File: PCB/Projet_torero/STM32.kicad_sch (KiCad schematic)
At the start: 34 parts, among them J1 Conn_02x07_Odd_Even, J201 Conn_02x08_Odd_Even, SW1 SW_Push, SW2 SW_Push, U1 STM32G431CBUx, Y1 Crystal_GND24_Small

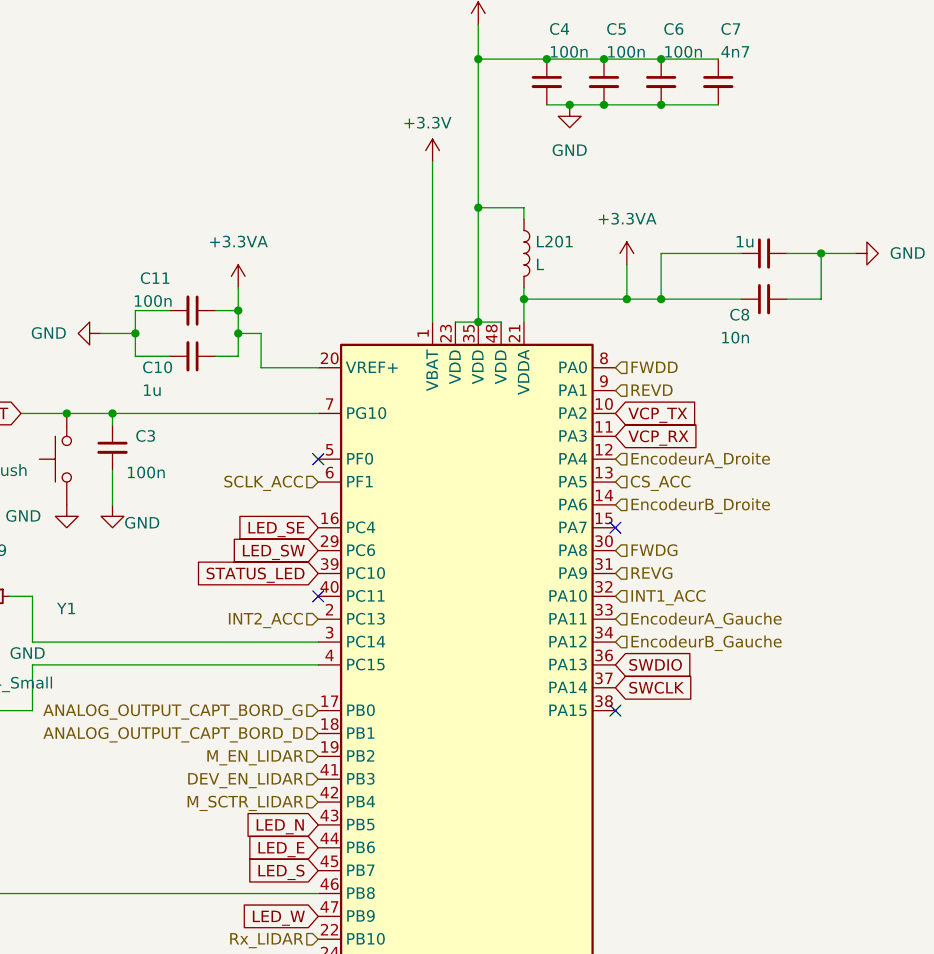
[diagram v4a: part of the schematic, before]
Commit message: changement pins STlink
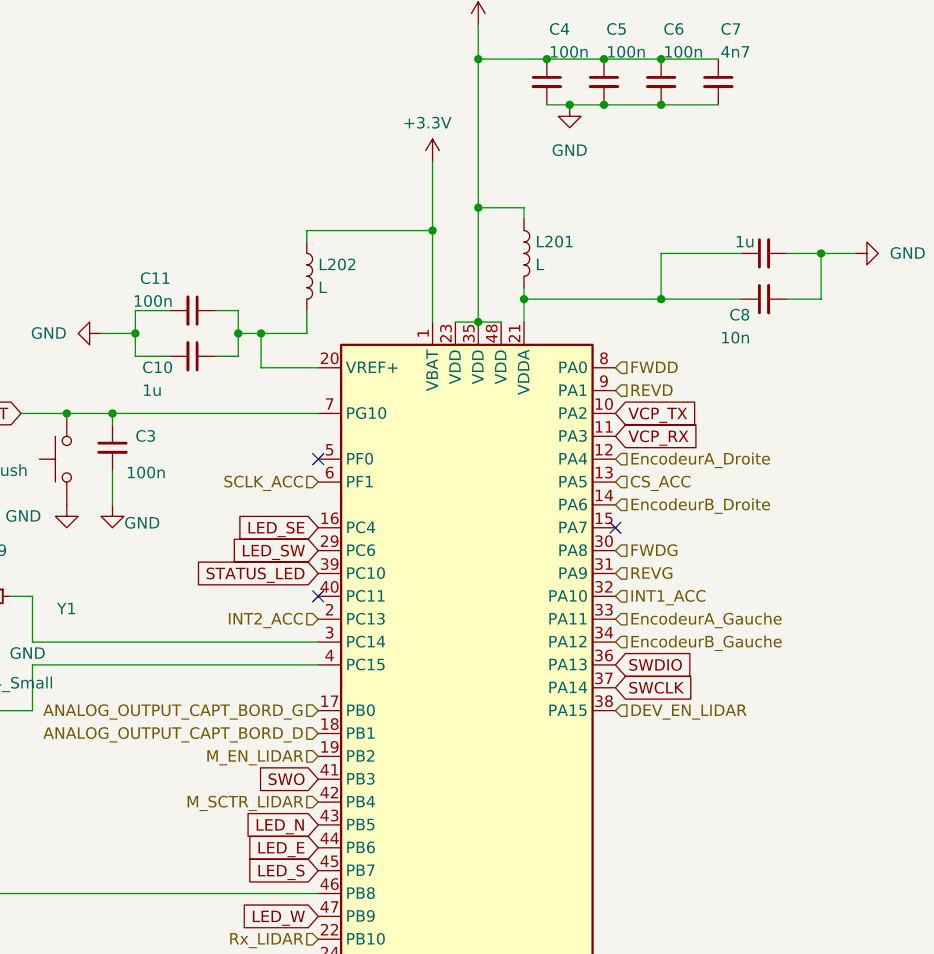
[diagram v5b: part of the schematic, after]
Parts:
- added L202: L, symbol Device:L
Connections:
- net +3.3V: now also L202.1
- net DEV_EN_LIDAR: now also U1.38 (PA15); no longer U1.41 (PB3)
- net SWO: now also U1.41 (PB3)
- net +3.3VA: no longer names the net of C8.1, C9.1, L201.2, U1.21 (VDDA)
- net +3.3VA: no longer C10.1, C11.1, U1.20 (VREF+)
- new net: C10.1, C11.1, L202.2, U1.20 (VREF+)
- no-connect marks 8 -> 7
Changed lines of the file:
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@@
 	)
 	(junction
-		(at 241.3 124.46)
+		(at 71.12 67.31)
 		(diameter 0)
 		(color 0 0 0 0)
 	)
 	(junction
-		(at 31.75 129.54)
+		(at 241.3 124.46)
 		(diameter 0)
 		(color 0 0 0 0)
 	)
 	(junction
-		(at 102.87 36.83)
+		(at 31.75 129.54)
 		(diameter 0)
 		(color 0 0 0 0)
 	)
 	(junction
-		(at 111.76 63.5)
+		(at 102.87 36.83)
 		(diameter 0)
 		(color 0 0 0 0)
 	)
 	(junction
-		(at 68.58 64.77)
+		(at 90.17 55.88)
 		(diameter 0)
 		(color 0 0 0 0)
@@
 	)
 	(no_connect
-		(at 110.49 109.22)
-	)
-	(no_connect
 		(at 110.49 88.9)
 	)
@@
 	(wire
 		(pts
+			(xy 90.17 55.88) (xy 90.17 66.04)
+		)
+		(stroke
+			(width 0)
+			(type default)
+		)
+	)
+	(wire
+		(pts
 			(xy 241.3 119.38) (xy 241.3 121.92)
 		)
@@
 	(wire
 		(pts
-			(xy 111.76 59.69) (xy 111.76 63.5)
+			(xy 90.17 48.26) (xy 90.17 55.88)
 		)
 		(stroke
@@
 	(wire
 		(pts
-			(xy 90.17 48.26) (xy 90.17 66.04)
+			(xy 95.25 36.83) (xy 95.25 53.34)
 		)
 		(stroke
@@
 	(wire
 		(pts
-			(xy 95.25 36.83) (xy 95.25 53.34)
+			(xy 76.2 64.77) (xy 76.2 67.31)
 		)
 		(stroke
@@
 	(wire
 		(pts
-			(xy 111.76 63.5) (xy 100.33 63.5)
+			(xy 100.33 63.5) (xy 115.57 63.5)
 		)
 		(stroke
@@
 	(wire
 		(pts
-			(xy 111.76 63.5) (xy 115.57 63.5)
+			(xy 241.3 134.62) (xy 241.3 137.16)
 		)
 		(stroke
@@
 	(wire
 		(pts
-			(xy 68.58 62.23) (xy 68.58 64.77)
+			(xy 45.72 104.14) (xy 45.72 109.22)
 		)
 		(stroke
@@
 	(wire
 		(pts
-			(xy 241.3 134.62) (xy 241.3 137.16)
+			(xy 222.25 127) (xy 224.79 127)
 		)
 		(stroke
@@
 		)
 	)
-	(wire
+	(polyline
 		(pts
-			(xy 45.72 104.14) (xy 45.72 109.22)
+			(xy 176.53 11.43) (xy 176.53 166.37)
 		)
 		(stroke
@@
 	(wire
 		(pts
-			(xy 222.25 127) (xy 224.79 127)
+			(xy 187.96 31.75) (xy 187.96 34.29)
 		)
 		(stroke
@@
 		)
 	)
-	(polyline
+	(wire
 		(pts
-			(xy 176.53 11.43) (xy 176.53 166.37)
+			(xy 203.2 68.58) (xy 203.2 72.39)
 		)
 		(stroke
@@
 	(wire
 		(pts
-			(xy 187.96 31.75) (xy 187.96 34.29)
+			(xy 105.41 41.91) (xy 109.22 41.91)
 		)
 		(stroke
@@
 	(wire
 		(pts
-			(xy 203.2 68.58) (xy 203.2 72.39)
+			(xy 35.56 105.41) (xy 35.56 109.22)
 		)
 		(stroke
@@
 	(wire
 		(pts
-			(xy 105.41 41.91) (xy 109.22 41.91)
+			(xy 115.57 36.83) (xy 121.92 36.83)
 		)
 		(stroke
@@
 	(wire
 		(pts
-			(xy 35.56 105.41) (xy 35.56 109.22)
+			(xy 241.3 121.92) (xy 241.3 124.46)
 		)
 		(stroke
@@
 	(wire
 		(pts
-			(xy 115.57 36.83) (xy 121.92 36.83)
+			(xy 76.2 55.88) (xy 76.2 57.15)
 		)
 		(stroke
@@
 	(wire
 		(pts
-			(xy 241.3 121.92) (xy 241.3 124.46)
+			(xy 35.56 96.52) (xy 35.56 100.33)
 		)
 		(stroke
@@
 	(wire
 		(pts
-			(xy 35.56 96.52) (xy 35.56 100.33)
+			(xy 124.46 58.42) (xy 115.57 58.42)
 		)
 		(stroke
@@
 	(wire
 		(pts
-			(xy 124.46 58.42) (xy 115.57 58.42)
+			(xy 76.2 67.31) (xy 71.12 67.31)
 		)
 		(stroke
@@
 	(wire
 		(pts
+			(xy 76.2 55.88) (xy 90.17 55.88)
+		)
+		(stroke
+			(width 0)
+			(type default)
+		)
+	)
+	(wire
+		(pts
 			(xy 241.3 119.38) (xy 237.49 119.38)
 		)
@@
 		)
 	)
+	(global_label "SWO"
+		(shape input)
+		(at 77.47 116.84 180)
+		(fields_autoplaced yes)
+		(effects
+			(font
+				(size 1.27 1.27)
+			)
+			(justify right)
+		)
+		(property "Intersheetrefs" "${INTERSHEET_REFS}"
+			(at 70.4934 116.84 0)
+			(effects
+				(font
+					(size 1.27 1.27)
+				)
+				(justify right)
+				(hide yes)
+			)
+		)
+	)
 	(global_label "VCP_RX"
 		(shape input)
@@
 	(hierarchical_label "DEV_EN_LIDAR"
 		(shape input)
-		(at 77.47 116.84 180)
+		(at 110.49 109.22 0)
 		(fields_autoplaced yes)
 		(effects
@@
 				(size 1.27 1.27)
 			)
-			(justify right)
+			(justify left)
 		)
 	)
@@
 	)
 	(symbol
-		(lib_id "power:+3.3VA")
-		(at 111.76 59.69 0)
-		(unit 1)
-		(exclude_from_sim no)
-		(in_bom yes)
-		(on_board yes)
-		(dnp no)
-		(fields_autoplaced yes)
-		(property "Reference" "#PWR031"
-			(at 111.76 63.5 0)
-			(effects
-				(font
-					(size 1.27 1.27)
-				)
-				(hide yes)
-			)
-		)
-		(property "Value" "+3.3VA"
-			(at 111.76 54.61 0)
-			(effects
-				(font
-					(size 1.27 1.27)
-				)
-			)
-		)
-		(property "Footprint" ""
-			(at 111.76 59.69 0)
-			(effects
-				(font
-					(size 1.27 1.27)
-				)
-				(hide yes)
-			)
-		)
-		(property "Datasheet" ""
-			(at 111.76 59.69 0)
-			(effects
-				(font
-					(size 1.27 1.27)
-				)
-				(hide yes)
-			)
-		)
-		(property "Description" "Power symbol creates a global label with name \"+3.3VA\""
-			(at 111.76 59.69 0)
-			(effects
-				(font
-					(size 1.27 1.27)
-				)
-				(hide yes)
-			)
-		)
-		(pin "1"
-		)
-		(instances
-			(project ""
-				(path "/04e1eb47-a2c4-462b-bef7-377d9515a2c0/6473f9d2-6a99-4702-8d30-7daa8ce98486"
-					(reference "#PWR031")
-					(unit 1)
-				)
-			)
-		)
-	)
-	(symbol
 		(lib_id "power:+3.3V")
 		(at 95.25 33.02 0)
@@
 	)
 	(symbol
-		(lib_id "power:+3.3VA")
-		(at 68.58 62.23 0)
-		(unit 1)
-		(exclude_from_sim no)
-		(in_bom yes)
-		(on_board yes)
-		(dnp no)
-		(fields_autoplaced yes)
-		(property "Reference" "#PWR032"
-			(at 68.58 66.04 0)
-			(effects
-				(font
-					(size 1.27 1.27)
-				)
-				(hide yes)
-			)
-		)
-		(property "Value" "+3.3VA"
-			(at 68.58 57.15 0)
-			(effects
-				(font
-					(size 1.27 1.27)
-				)
-			)
-		)
-		(property "Footprint" ""
-			(at 68.58 62.23 0)
-			(effects
-				(font
-					(size 1.27 1.27)
-				)
-				(hide yes)
-			)
-		)
-		(property "Datasheet" ""
-			(at 68.58 62.23 0)
-			(effects
-				(font
-					(size 1.27 1.27)
-				)
-				(hide yes)
-			)
-		)
-		(property "Description" "Power symbol creates a global label with name \"+3.3VA\""
-			(at 68.58 62.23 0)
-			(effects
-				(font
-					(size 1.27 1.27)
-				)
-				(hide yes)
-			)
-		)
-		(pin "1"
-		)
-		(instances
-			(project "Projet_torero"
-				(path "/04e1eb47-a2c4-462b-bef7-377d9515a2c0/6473f9d2-6a99-4702-8d30-7daa8ce98486"
-					(reference "#PWR032")
-					(unit 1)
-				)
-			)
-		)
-	)
-	(symbol
 		(lib_id "Device:C_Small")
 		(at 26.67 96.52 90)
@@
 					(unit 1)
 				)
+			)
+		)
+	)
+	(symbol
+		(lib_id "Device:L")
+		(at 76.2 60.96 0)
+		(unit 1)
+		(exclude_from_sim no)
+		(in_bom yes)
+		(on_board yes)
+		(dnp no)
+		(fields_autoplaced yes)
+		(property "Reference" "L202"
+			(at 77.47 59.6899 0)
+			(effects
+				(font
+					(size 1.27 1.27)
+				)
+				(justify left)
+			)
+		)
+		(property "Value" "L"
+			(at 77.47 62.2299 0)
+			(effects
+				(font
+					(size 1.27 1.27)
+				)
+				(justify left)
+			)
+		)
+		(property "Footprint" ""
+			(at 76.2 60.96 0)
+			(effects
+				(font
+					(size 1.27 1.27)
+				)
+				(hide yes)
+			)
+		)
+		(property "Datasheet" "~"
+			(at 76.2 60.96 0)
+			(effects
+				(font
+					(size 1.27 1.27)
+				)
+				(hide yes)
+			)
+		)
+		(property "Description" "Inductor"
+			(at 76.2 60.96 0)
+			(effects
+				(font
+					(size 1.27 1.27)
+				)
+				(hide yes)
+			)
+		)
+		(pin "1"
+		)
+		(pin "2"
+		)
+		(instances
+			(project "Projet_torero"
+				(path "/04e1eb47-a2c4-462b-bef7-377d9515a2c0/6473f9d2-6a99-4702-8d30-7daa8ce98486"
+					(reference "L202")
+					(unit 1)
+				)

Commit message: changement schéma
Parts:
- renumbered 10k to 10k201, C1 to C201, C2 to C202, C3 to C203, C11 to C204, C10 to C205, C4 to C206, C5 to C207, C6 to C208, C7 to C209, C9 to C210, C8 to C211, D1 to D201, D2 to D202, J1 to J201, J201 to J202, JP1 to JP201, JP2 to JP202, L202 to L201, L201 to L202, R209 to R201, R3 to R202, R4 to R203, R201 to R204, R202 to R205, R203 to R206, R204 to R207, R205 to R208, R206 to R209, R207 to R210, R208 to R211, SW1 to SW201, SW2 to SW202, U1 to U201, Y1 to Y201

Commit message: maj pin STM
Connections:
- net SCLK_ACC is gone; now on an unnamed net: U201.6 (PF1)
- net GND: now also C202.2; no longer C202.1
- net LED_NE: now also U201.15 (PA7); no longer U201.25 (PB12)
- net LED_NW: now also U201.25 (PB12); no longer U201.26 (PB13)
- net LED_W: now also U201.42 (PB4); no longer U201.47 (PB9)
- net M_SCTR_LIDAR: now also U201.47 (PB9); no longer U201.42 (PB4)
- net at R201.1: no longer U201.3 (PC14)
- net at U201.5 (PF0): now also C202.1, Y201.1
- new net SPI2_SCK: U201.26 (PB13)
- now unconnected: U201.4 (PC15)
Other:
- moved on the sheet: C201, C202, R201, Y201

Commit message: Re-Push pour les empreintes et le PCB
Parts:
- removed JP201, JP202: SolderJumper_2_Open, Jumper:SolderJumper-2_P1.3mm_Open_TrianglePad1.0x1.5mm, symbol Jumper:SolderJumper_2_Open
- removed L201: L, symbol Device:L
- 10k201, R204, R205, R206, R207, R208, R209, R210, R211: footprint (none) -> Resistor_SMD:R_0603_1608Metric
- C201, C202, C203, C204, C206, C207, C208, C211: footprint (none) -> Capacitor_SMD:C_0402_1005Metric
- C205, C209, C210: footprint (none) -> Capacitor_SMD:C_0603_1608Metric
- J201: footprint (none) -> Connector_PinHeader_1.27mm:PinHeader_2x07_P1.27mm_Vertical_SMD
- J202: footprint (none) -> Connector_PinHeader_1.27mm:PinHeader_2x08_P1.27mm_Vertical_SMD
- L202: footprint (none) -> Inductor_SMD:L_0603_1608Metric_Pad1.05x0.95mm_HandSolder
- R201, R202, R203: footprint Resistor_SMD:R_0603_1608Metric_Pad0.98x0.95mm_HandSolder -> Resistor_SMD:R_0603_1608Metric
- SW201, SW202: footprint (none) -> Button_Switch_SMD:SW_Push_1P1T_NO_6x6mm_H9.5mm
- Y201: footprint (none) -> Crystal:Crystal_SMD_EuroQuartz_X22-4Pin_2.5x2.0mm
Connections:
- net +3.3V: now also C204.1, C205.1, C210.1, C211.1, L202.2, U201.20 (VREF+), U201.21 (VDDA)
- net VCP_RX: now also J201.13 (Pin_13)
- net VCP_TX: now also J201.14 (Pin_14)
